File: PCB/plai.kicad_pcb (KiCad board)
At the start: 2 copper layers, 83.9 x 80 mm, 22 parts, among them SW1 SW_Push, SW10 RotaryEncoder_Switch, SW2 SW_Push, SW3 SW_Push, SW4 SW_Push, SW5 SW_Push, SW6 SW_Push, SW7 SW_Push, SW8 SW_Push, SW9 SW_Push, U1 ER_OLEDM0.91_1x-I2C, U2 MOUDLE-SEEEDUINO-XIAO

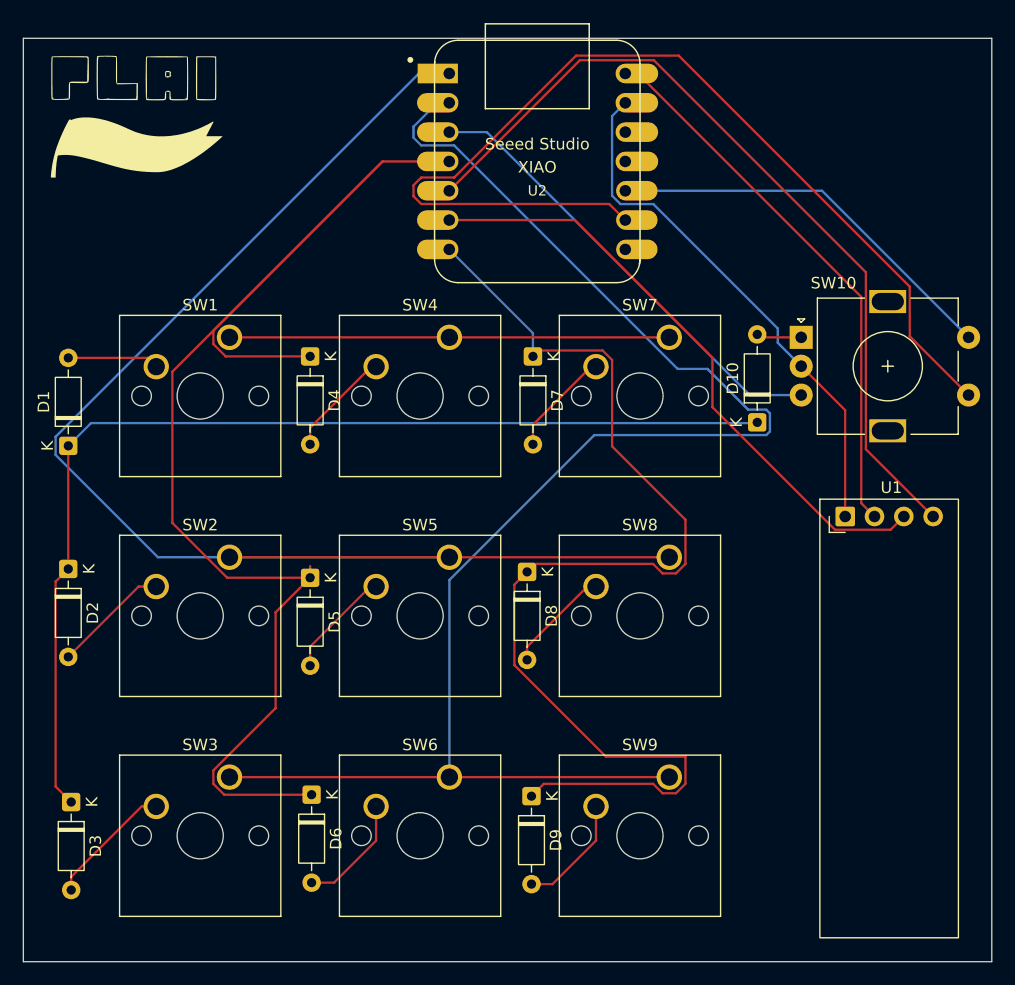
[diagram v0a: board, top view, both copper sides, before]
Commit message: Fullyt Routed PCB Beautifully Routed + Some additions ot the firmware
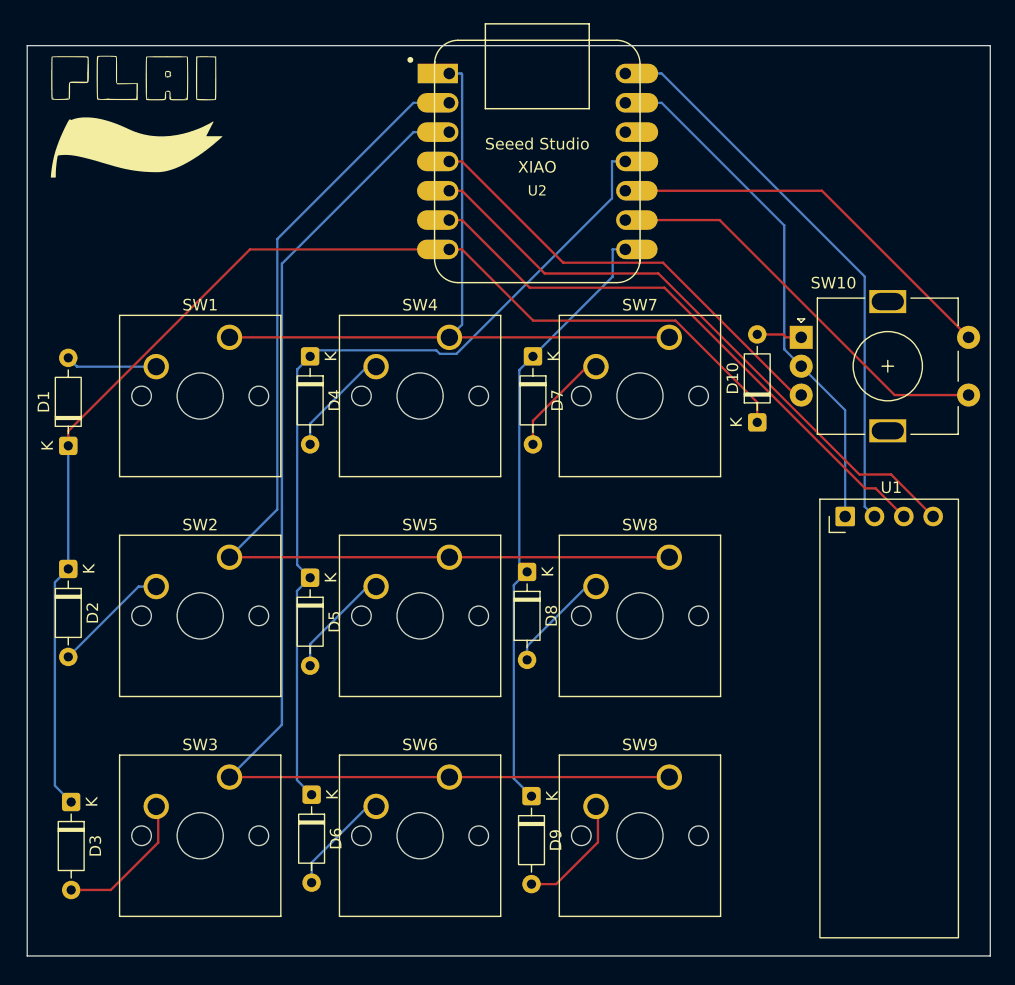
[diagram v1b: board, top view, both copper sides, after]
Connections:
- net /SCL renamed SCL
- net /SDA renamed SDA
- U2 pad 1: COL1 -> COL0
- U2 pad 11: unconnected-(U2-PA6_A10_D10_MOSI-Pad11) -> ROW1
- U2 pad 2: COL2 -> COL1
- U2 pad 3: COL3 -> COL2
- U2 pad 4: ROW1 -> COL3
- U2 pad 7: ROW2 -> ROW0
- U2 pad 8: /ROW3 -> ROW2
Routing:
- net EC11A: track 87.6 -> 36.0 mm
- net ROW2: track 98.1 -> 53.2 mm
- net ROW1: track 121.1 -> 76.3 mm
- net COL1: track 124.6 -> 87.2 mm
- net COL2: track 135.5 -> 103.7 mm
- net COL0: track 38.1 -> 62.5 mm
- net SDA: track 72.0 -> 53.6 mm
- net ROW0: track 92.4 -> 106.6 mm
- net SCL: track 53.5 -> 50.0 mm
- net Net-(D3-A): track 11.0 -> 12.4 mm
- net VCC: track 48.0 -> 49.2 mm
- net COL3: track 39.9 -> 38.9 mm
- net GND: track 46.4 -> 45.6 mm
- net Net-(D6-A): track 10.1 -> 9.34 mm
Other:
- board size 83.9 x 80 mm -> 83.4 x 78.9 mm
